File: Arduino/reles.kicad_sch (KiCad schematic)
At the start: 2 parts, among them J14 Screw_Terminal_01x12

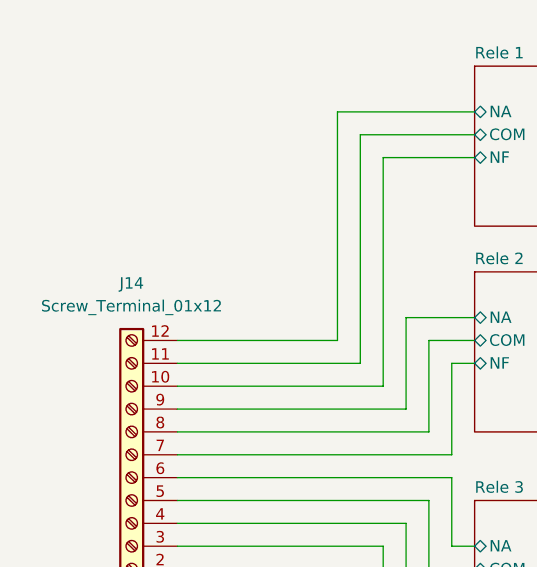
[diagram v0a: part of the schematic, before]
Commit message: Added all components to arduino pcb.
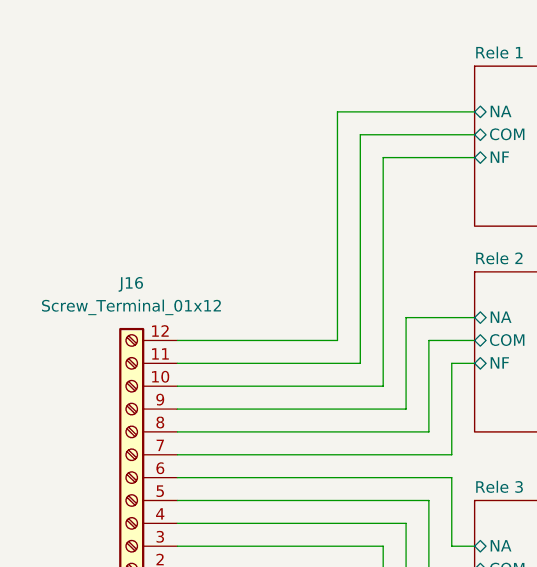
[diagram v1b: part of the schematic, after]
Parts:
- renumbered J14 to J16
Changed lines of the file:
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@@
 		(dnp no)
 		(fields_autoplaced yes)
-		(property "Reference" "J14"
+		(property "Reference" "J16"
 			(at 91.44 80.01 0)
 			(effects
@@
 			(project ""
 				(path "/b1260de1-9c48-4b08-a759-f31e40d6183e/6d409481-8893-4a65-ac5a-8215d51ff4b9"
-					(reference "J14")
+					(reference "J16")
 					(unit 1)
 				)

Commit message: First version from PCB schematic.
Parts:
- J16: footprint TerminalBlock_RND:TerminalBlock_RND_205-00297_1x12_P5.08mm_Horizontal -> TerminalBlock_Phoenix:TerminalBlock_Phoenix_PT-1,5-12-5.0-H_1x12_P5.00mm_Horizontal
- renumbered JP2 to JP3
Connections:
- net Rele 1/COM: now also J16.2 (Pin_2); no longer J16.11 (Pin_11)
- net Rele 1/NA: now also J16.1 (Pin_1); no longer J16.12 (Pin_12)
- net Rele 1/NF: now also J16.3 (Pin_3); no longer J16.10 (Pin_10)
- net Rele 2/COM: now also J16.5 (Pin_5); no longer J16.8 (Pin_8)
- net Rele 2/NA: now also J16.4 (Pin_4); no longer J16.9 (Pin_9)
- net Rele 2/NF: now also J16.6 (Pin_6); no longer J16.7 (Pin_7)
- net Rele 3/COM: now also J16.8 (Pin_8); no longer J16.5 (Pin_5)
- net Rele 3/NA: now also J16.7 (Pin_7); no longer J16.6 (Pin_6)
- net Rele 3/NF: now also J16.9 (Pin_9); no longer J16.4 (Pin_4)
- net Rele 4/COM: now also J16.11 (Pin_11); no longer J16.2 (Pin_2)
- net Rele 4/NA: now also J16.10 (Pin_10); no longer J16.3 (Pin_3)
- net Rele 4/NF: now also J16.12 (Pin_12); no longer J16.1 (Pin_1)
- net 12V renamed +12V
- net 5V renamed +5V
- net Rele 1/12V renamed Rele 1/+12V
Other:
- sheet Rele 1 ports: added +12V; removed 12V
- sheet Rele 2 ports: added +12V; removed 12V
- sheet Rele 3 ports: added +12V; removed 12V
- sheet Rele 4 ports: added +12V; removed 12V
- moved on the sheet: J16
